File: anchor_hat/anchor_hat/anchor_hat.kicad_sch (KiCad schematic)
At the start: 37 parts, among them J1 GPIO, J2 Motor 1, J3 Motor 2, J4 24v in barrel jack, J5 24v out slip ring, J7 5v out fan right angle, Q1 AOD4185, Q3 2N7002, U2 MCP2515-xST, U3 SN65HVD230, U4 TPS54302, Y1 12M

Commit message: Layout board with mosfet, pwm fan
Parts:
- added J6: 5v pwm fan, Connector_JST:JST_SH_SM04B-SRSS-TB_1x04-1MP_P1.00mm_Horizontal, symbol Connector:Conn_01x04_Socket
- added R13: 10kOhm, Resistor_SMD:R_0603_1608Metric, symbol Device:R_US
- added R14: 1kOhm, Resistor_SMD:R_0603_1608Metric, symbol Device:R_US
- added R15: 100 Ohm, Resistor_SMD:R_0603_1608Metric, symbol Device:R_US
- J7: value 5v out fan right angle -> 5v out fan (DNP); footprint Connector_PinHeader_2.54mm:PinHeader_1x02_P2.54mm_Horizontal -> Connector_JST:JST_PH_B2B-PH-K_1x02_P2.00mm_Vertical; now not fitted
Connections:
- net +3.3V: now also R13.1
- net +5V: now also J6.1 (Pin_1)
- net GND: now also U2.10 (VSS), J6.3 (Pin_3)
- net GPIO12/PWM0: now also R15.1
- net GPIO16: now also R13.2, R14.1
- new net: J6.2 (Pin_2), R15.2
- new net: J6.4 (Pin_4), R14.2
- no-connect marks 0 -> 7

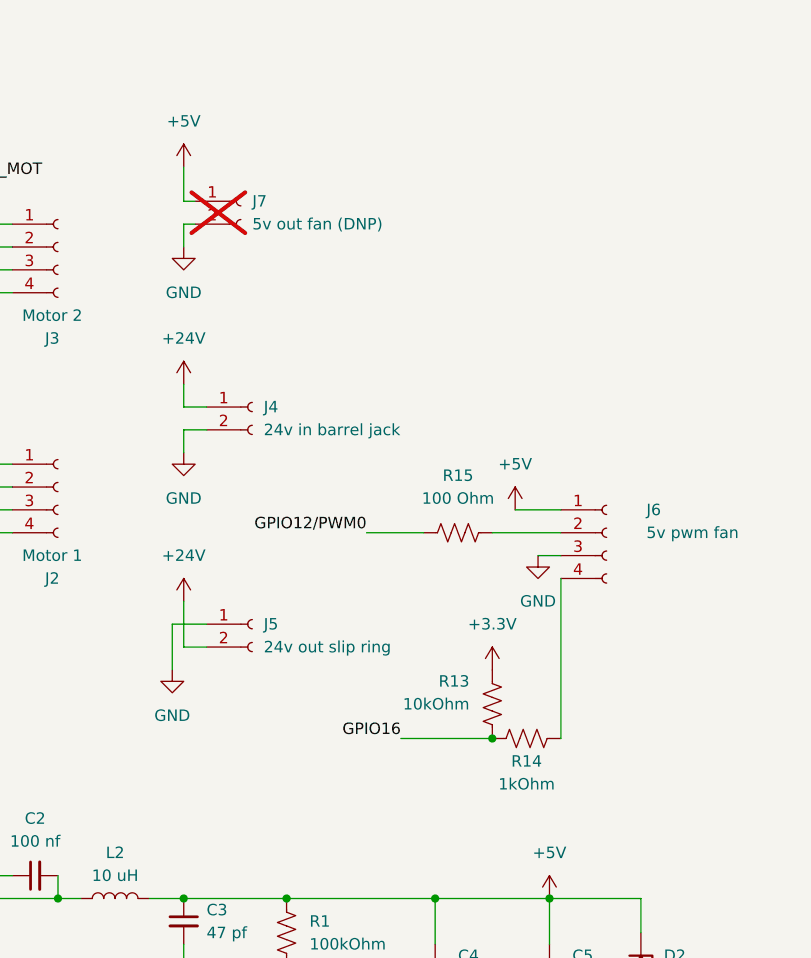
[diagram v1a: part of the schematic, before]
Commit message: replace 4 wire fan with 2 wire fan and pwm control
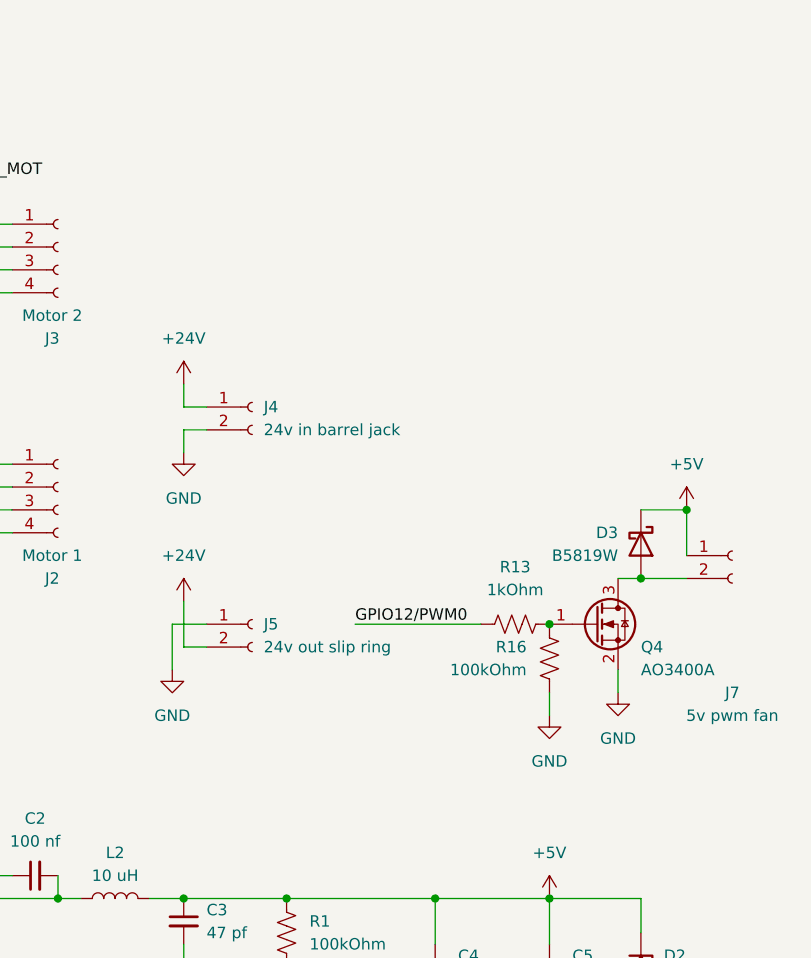
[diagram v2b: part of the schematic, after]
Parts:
- removed J6: 5v pwm fan, Connector_JST:JST_SH_SM04B-SRSS-TB_1x04-1MP_P1.00mm_Horizontal, symbol Connector:Conn_01x04_Socket
- removed R14: 1kOhm, Resistor_SMD:R_0603_1608Metric, symbol Device:R_US
- removed R15: 100 Ohm, Resistor_SMD:R_0603_1608Metric, symbol Device:R_US
- added D3: B5819W, Diode_SMD:D_SOD-123, symbol Device:D_Schottky
- added Q4: AO3400A, Package_TO_SOT_SMD:SOT-23, symbol Transistor_FET:AO3400A
- added R16: 100kOhm, Resistor_SMD:R_0603_1608Metric, symbol Device:R_US
- J7: value 5v out fan (DNP) -> 5v pwm fan; now fitted
- R13: value 10kOhm -> 1kOhm
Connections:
- net +3.3V: no longer R13.1
- net +5V: now also D3.1 (K)
- net GND: now also Q4.2 (S), R16.2; no longer J7.2 (Pin_2)
- net GPIO12/PWM0: now also R13.1
- net GPIO16: no longer R13.2
- new net: Q4.1 (G), R13.2, R16.1
- new net: D3.2 (A), J7.2 (Pin_2), Q4.3 (D)
